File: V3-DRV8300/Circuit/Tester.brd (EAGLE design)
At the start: 27.9 x 34.9 mm, 27 parts, among them IC1 DRV8303DCA

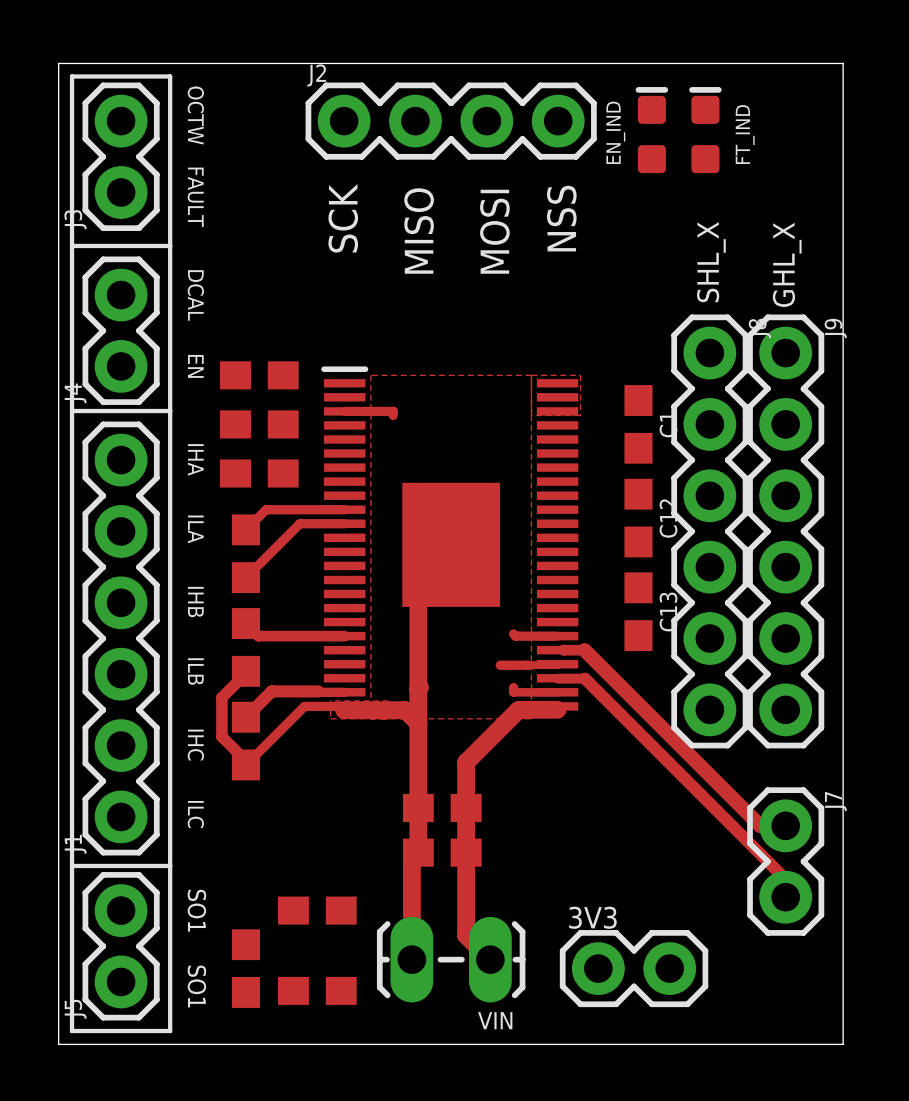
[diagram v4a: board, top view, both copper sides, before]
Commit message: Ready for autoroutering (Tester) 6
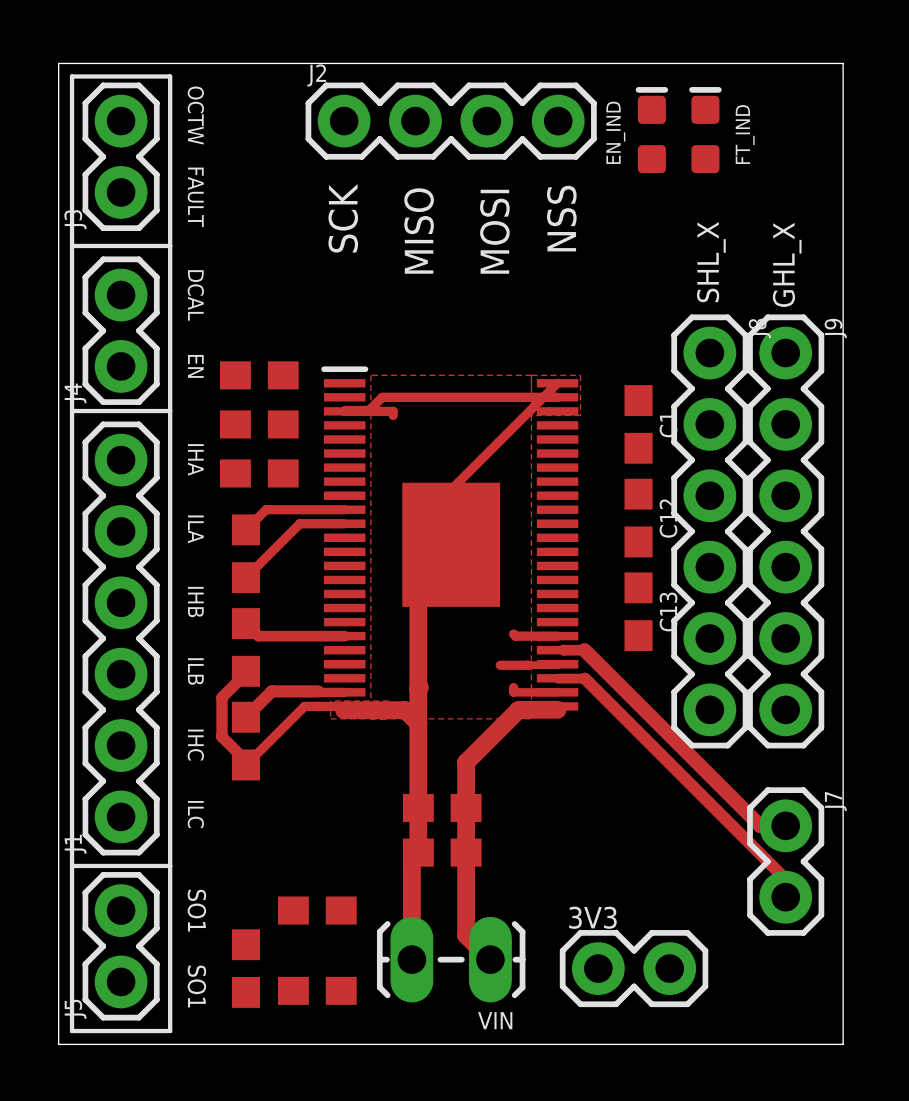
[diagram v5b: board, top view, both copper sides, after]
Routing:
- net GND: track 34.0 -> 49.1 mm
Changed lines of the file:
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@@
 <wire x1="17.758" y1="14.53" x2="16.2675" y2="14.53" width="0.3302" layer="1"/>
 <wire x1="16.2675" y1="14.53" x2="16.1925" y2="14.605" width="0.3302" layer="1"/>
+<wire x1="11.0510125" y1="22.5625" x2="10.2145" y2="22.5625" width="0.3302" layer="1"/>
+<wire x1="10.2145" y1="22.5625" x2="10.182" y2="22.53" width="0.3302" layer="1"/>
+<wire x1="17.758" y1="23.03" x2="11.5185125" y2="23.03" width="0.3302" layer="1"/>
+<wire x1="11.5185125" y1="23.03" x2="11.0510125" y2="22.5625" width="0.3302" layer="1"/>
+<wire x1="17.758" y1="23.53" x2="13.97" y2="19.742" width="0.3302" layer="1"/>
+<wire x1="13.97" y1="19.742" x2="13.97" y2="17.78" width="0.3302" layer="1"/>
 <wire x1="21.11375" y1="33.262" x2="23.01875" y2="33.262" width="0" layer="19" extent="1-1"/>
-<wire x1="17.758" y1="23.53" x2="21.11375" y2="33.262" width="0" layer="19" extent="1-1"/>
+<wire x1="13.97" y1="17.78" x2="21.11375" y2="33.262" width="0" layer="19" extent="1-1"/>
 <wire x1="6.29375" y1="20.32" x2="10.182" y2="22.53" width="0" layer="19" extent="1-1"/>
 <wire x1="23.1775" y1="11.90625" x2="17.758" y2="12.53" width="0" layer="19" extent="1-1"/>

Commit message: Ready for autoroutering (Tester) 7
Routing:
- net GND: track 49.1 -> 52.7 mm
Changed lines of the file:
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@@
 <wire x1="12.8025" y1="11.43" x2="12.3375" y2="11.895" width="0.635" layer="1"/>
 <wire x1="12.3375" y1="11.895" x2="10.16" y2="11.895" width="0.635" layer="1"/>
-<wire x1="12.8025" y1="12.64375" x2="12.8025" y2="16.6125" width="0.635" layer="1"/>
 <wire x1="12.8025" y1="16.6125" x2="13.97" y2="17.78" width="0.635" layer="1"/>
 <wire x1="17.758" y1="14.53" x2="16.2675" y2="14.53" width="0.3302" layer="1"/>
@@
 <wire x1="11.5185125" y1="23.03" x2="11.0510125" y2="22.5625" width="0.3302" layer="1"/>
 <wire x1="17.758" y1="23.53" x2="13.97" y2="19.742" width="0.3302" layer="1"/>
-<wire x1="13.97" y1="19.742" x2="13.97" y2="17.78" width="0.3302" layer="1"/>
+<wire x1="13.97" y1="19.742" x2="13.97" y2="17.93875" width="0.3302" layer="1"/>
+<wire x1="13.97" y1="17.93875" x2="13.97" y2="17.78" width="0.3302" layer="1"/>
+<wire x1="12.8025" y1="11.43" x2="14.0725" y2="12.7" width="0.3302" layer="1"/>
+<wire x1="14.0725" y1="12.7" x2="14.44625" y2="12.7" width="0.3302" layer="1"/>
+<wire x1="14.44625" y1="12.7" x2="14.44625" y2="17.4625" width="0.3302" layer="1"/>
+<wire x1="14.44625" y1="17.4625" x2="13.97" y2="17.93875" width="0.3302" layer="1"/>
 <wire x1="21.11375" y1="33.262" x2="23.01875" y2="33.262" width="0" layer="19" extent="1-1"/>
-<wire x1="13.97" y1="17.78" x2="21.11375" y2="33.262" width="0" layer="19" extent="1-1"/>
+<wire x1="17.758" y1="23.53" x2="21.11375" y2="33.262" width="0" layer="19" extent="1-1"/>
 <wire x1="6.29375" y1="20.32" x2="10.182" y2="22.53" width="0" layer="19" extent="1-1"/>
 <wire x1="23.1775" y1="11.90625" x2="17.758" y2="12.53" width="0" layer="19" extent="1-1"/>

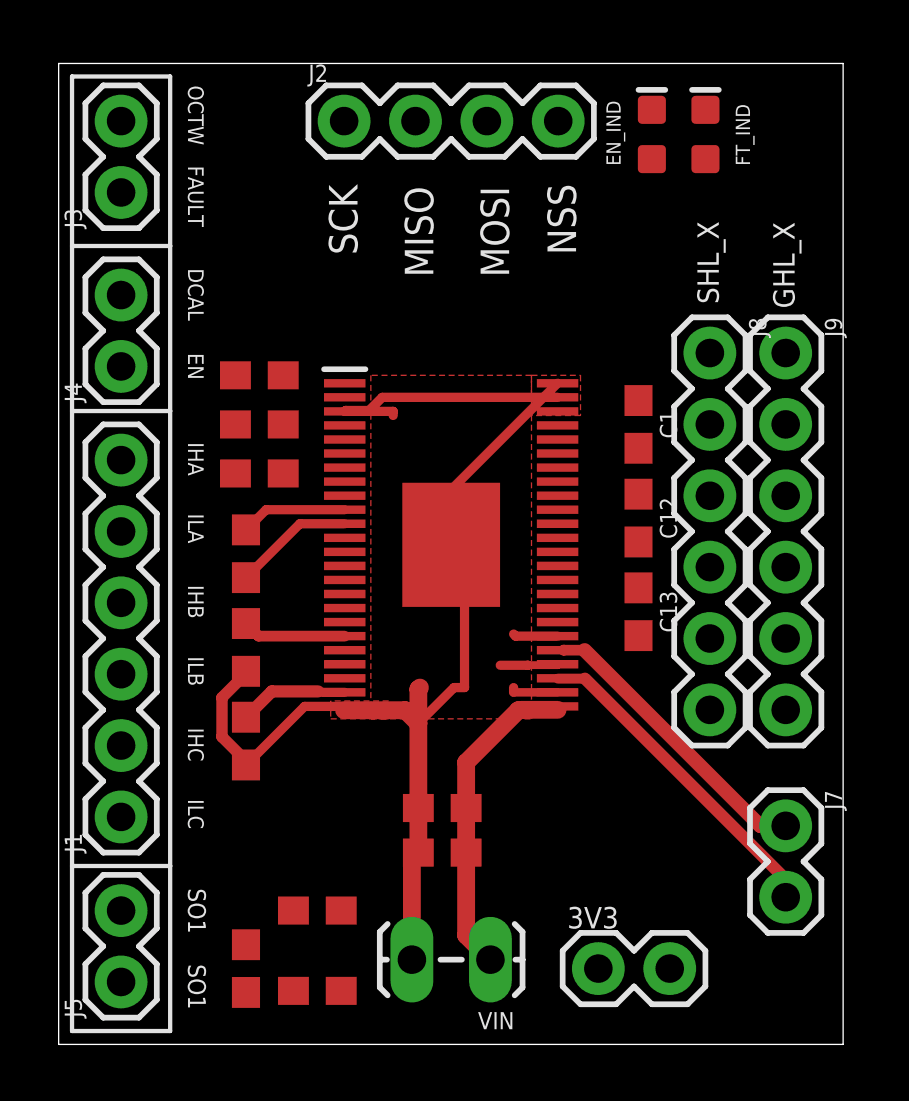
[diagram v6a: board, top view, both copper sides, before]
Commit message: Autoroutered the tester board
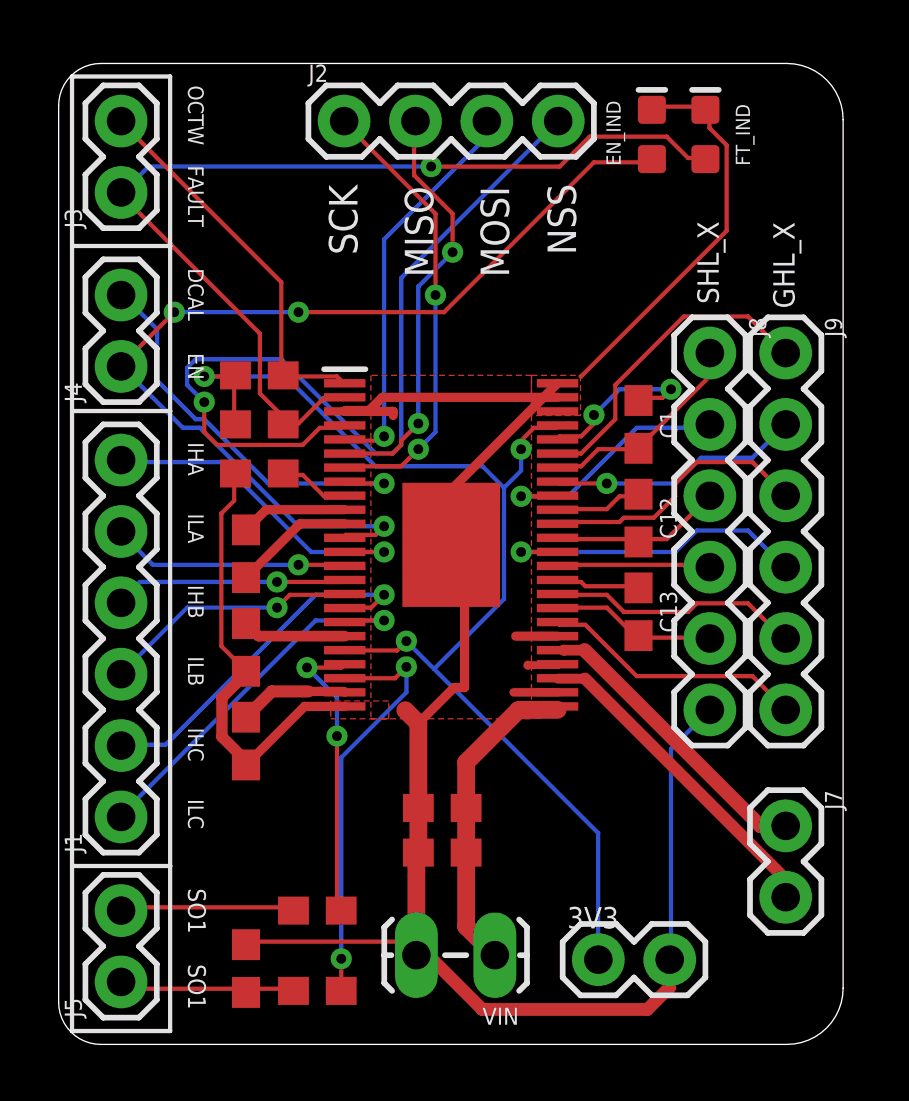
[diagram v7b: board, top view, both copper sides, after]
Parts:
- moved J6 0.32 mm to (19.2, 3.02)
- moved VIN 0.22 mm to (12.9, 3.17)
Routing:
- net GND: track 52.7 -> 96.9 mm
- net VCC: track 0.00 -> 42.6 mm, vias 0 -> 3
- net EN_GATE: track 0.00 -> 35.3 mm, vias 0 -> 3
- net N_FAULT: track 0.00 -> 35.2 mm, vias 0 -> 1
- net N_SCS: track 0.00 -> 31.1 mm, vias 0 -> 1
- net SCLK: track 0.00 -> 16.2 mm, vias 0 -> 2
- net SDO: track 0.00 -> 15.0 mm, vias 0 -> 2
- net N$3: track 0.00 -> 14.9 mm, vias 0 -> 2
- net DC_CAL: track 0.00 -> 14.7 mm, vias 0 -> 1
- net SDI: track 0.00 -> 14.2 mm, vias 0 -> 1
- net INLC: track 0.00 -> 13.7 mm, vias 0 -> 1
- net N_OCTW: track 0.00 -> 13.7 mm
- net INHC: track 0.00 -> 13.2 mm, vias 0 -> 1
- net INHA: track 0.00 -> 12.1 mm, vias 0 -> 1
- net GL_B: track 0.00 -> 11.6 mm, vias 0 -> 1
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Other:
- outline, holes or cut-outs redrawn
